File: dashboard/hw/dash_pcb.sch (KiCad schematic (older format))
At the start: 28 parts, among them J1 LCD, J2 DEBUG, J3 LCD_BL, J4 CAN, J5 POWER, U1 LPC11C24FBD48, U2 TPS62175

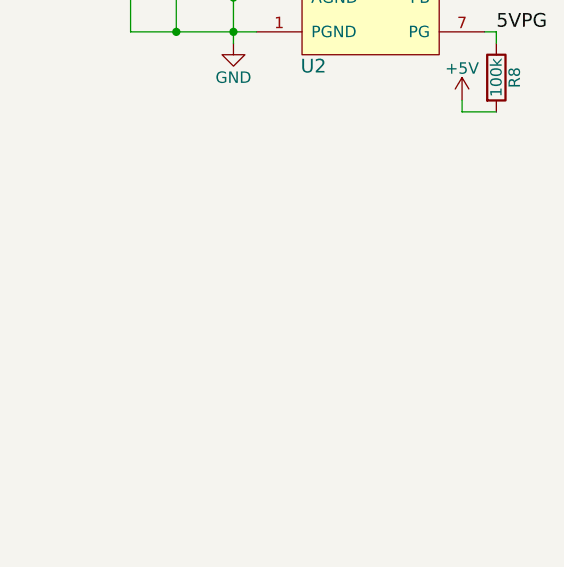
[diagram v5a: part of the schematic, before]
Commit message: add 3v3 power supply
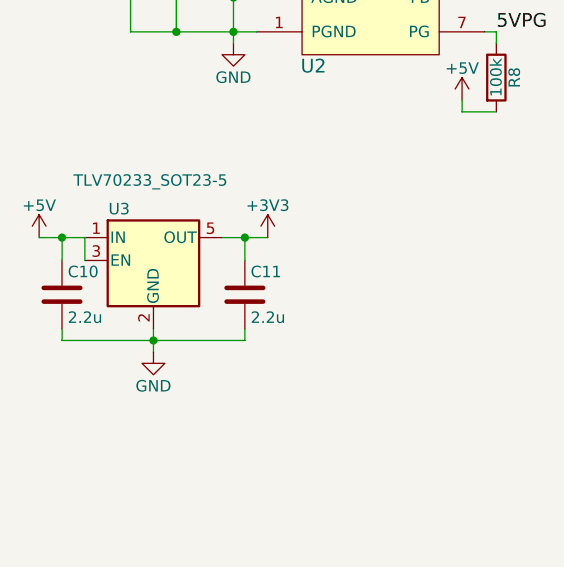
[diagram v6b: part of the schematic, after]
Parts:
- added C10, C11: 2.2u, Capacitors_SMD:C_0603, symbol C
- added U3: TLV70233_SOT23-5, TO_SOT_Packages_SMD:SOT-23-5, symbol TLV70233_SOT23-5
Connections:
- net +3V3: now also C11.1, U3.5 (OUT)
- net +5V: now also C10.1, U3.1 (IN), U3.3 (EN)
- net GND: now also C10.2, C11.2, U3.2 (GND)
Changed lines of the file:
@@
 $EndComp
 $Comp
-L GND #PWR16
+L GND #PWR19
 U 1 1 5ADCA1A0
 P 9250 2600
-F 0 "#PWR16" H 9250 2350 50  0001 C CNN
+F 0 "#PWR19" H 9250 2350 50  0001 C CNN
 F 1 "GND" H 9250 2450 50  0000 C CNN
 F 2 "" H 9250 2600 50  0001 C CNN
@@
 LCD_VEE
 $Comp
-L GND #PWR7
+L GND #PWR10
 U 1 1 5ADCA50B
 P 5450 5450
-F 0 "#PWR7" H 5450 5200 50  0001 C CNN
+F 0 "#PWR10" H 5450 5200 50  0001 C CNN
 F 1 "GND" H 5450 5300 50  0000 C CNN
 F 2 "" H 5450 5450 50  0001 C CNN
@@
 $EndComp
 $Comp
-L GND #PWR12
+L GND #PWR15
 U 1 1 5ADCA542
 P 7300 4850
-F 0 "#PWR12" H 7300 4600 50  0001 C CNN
+F 0 "#PWR15" H 7300 4600 50  0001 C CNN
 F 1 "GND" H 7300 4700 50  0000 C CNN
 F 2 "" H 7300 4850 50  0001 C CNN
@@
 $EndComp
 $Comp
-L +3V3 #PWR8
+L +3V3 #PWR11
 U 1 1 5ADCA654
 P 5600 1800
-F 0 "#PWR8" H 5600 1650 50  0001 C CNN
+F 0 "#PWR11" H 5600 1650 50  0001 C CNN
 F 1 "+3V3" H 5600 1940 50  0000 C CNN
 F 2 "" H 5600 1800 50  0001 C CNN
@@
 $EndComp
 $Comp
-L +5V #PWR11
+L +5V #PWR14
 U 1 1 5ADCA762
 P 7300 4550
-F 0 "#PWR11" H 7300 4400 50  0001 C CNN
+F 0 "#PWR14" H 7300 4400 50  0001 C CNN
 F 1 "+5V" H 7300 4690 50  0000 C CNN
 F 2 "" H 7300 4550 50  0001 C CNN
@@
 $EndComp
 $Comp
-L +3V3 #PWR18
+L +3V3 #PWR21
 U 1 1 5ADCAB0C
 P 9500 5650
-F 0 "#PWR18" H 9500 5500 50  0001 C CNN
+F 0 "#PWR21" H 9500 5500 50  0001 C CNN
 F 1 "+3V3" H 9500 5790 50  0000 C CNN
 F 2 "" H 9500 5650 50  0001 C CNN
@@
 $EndComp
 $Comp
-L GND #PWR17
+L GND #PWR20
 U 1 1 5ADCAB42
 P 9350 6300
-F 0 "#PWR17" H 9350 6050 50  0001 C CNN
+F 0 "#PWR20" H 9350 6050 50  0001 C CNN
 F 1 "GND" H 9350 6150 50  0000 C CNN
 F 2 "" H 9350 6300 50  0001 C CNN
@@
 CANL
 $Comp
-L +3V3 #PWR15
+L +3V3 #PWR18
 U 1 1 5AE5BC1B
 P 8800 2600
-F 0 "#PWR15" H 8800 2450 50  0001 C CNN
+F 0 "#PWR18" H 8800 2450 50  0001 C CNN
 F 1 "+3V3" H 8800 2740 50  0000 C CNN
 F 2 "" H 8800 2600 50  0001 C CNN
@@
 $EndComp
 $Comp
-L +3V3 #PWR14
+L +3V3 #PWR17
 U 1 1 5AE5BE05
 P 8450 3700
-F 0 "#PWR14" H 8450 3550 50  0001 C CNN
+F 0 "#PWR17" H 8450 3550 50  0001 C CNN
 F 1 "+3V3" H 8450 3840 50  0000 C CNN
 F 2 "" H 8450 3700 50  0001 C CNN
@@
 $EndComp
 $Comp
-L GND #PWR13
+L GND #PWR16
 U 1 1 5AE5BE6A
 P 8450 3100
-F 0 "#PWR13" H 8450 2850 50  0001 C CNN
+F 0 "#PWR16" H 8450 2850 50  0001 C CNN
 F 1 "GND" H 8450 2950 50  0000 C CNN
 F 2 "" H 8450 3100 50  0001 C CNN
@@
 $EndComp
 $Comp
-L GND #PWR21
+L GND #PWR24
 U 1 1 5AE5C42C
 P 10850 2800
-F 0 "#PWR21" H 10850 2550 50  0001 C CNN
+F 0 "#PWR24" H 10850 2550 50  0001 C CNN
 F 1 "GND" H 10850 2650 50  0000 C CNN
 F 2 "" H 10850 2800 50  0001 C CNN
@@
 $EndComp
 $Comp
-L GND #PWR19
+L GND #PWR22
 U 1 1 5AED81B0
 P 10000 4950
-F 0 "#PWR19" H 10000 4700 50  0001 C CNN
+F 0 "#PWR22" H 10000 4700 50  0001 C CNN
 F 1 "GND" H 10000 4800 50  0000 C CNN
 F 2 "" H 10000 4950 50  0001 C CNN
@@
 $EndComp
 $Comp
-L GND #PWR20
+L GND #PWR23
 U 1 1 5AED81E8
 P 10450 4450
-F 0 "#PWR20" H 10450 4200 50  0001 C CNN
+F 0 "#PWR23" H 10450 4200 50  0001 C CNN
 F 1 "GND" H 10450 4300 50  0000 C CNN
 F 2 "" H 10450 4450 50  0001 C CNN
@@
 $EndComp
 $Comp
-L GND #PWR10
+L GND #PWR13
 U 1 1 5AED9C6E
 P 6900 4400
-F 0 "#PWR10" H 6900 4150 50  0001 C CNN
+F 0 "#PWR13" H 6900 4150 50  0001 C CNN
 F 1 "GND" H 6900 4250 50  0000 C CNN
 F 2 "" H 6900 4400 50  0001 C CNN
@@
 $EndComp
 $Comp
-L GND #PWR9
+L GND #PWR12
 U 1 1 5AEDA2F6
 P 6050 2550
-F 0 "#PWR9" H 6050 2300 50  0001 C CNN
+F 0 "#PWR12" H 6050 2300 50  0001 C CNN
 F 1 "GND" H 6050 2400 50  0000 C CNN
 F 2 "" H 6050 2550 50  0001 C CNN
@@
 $EndComp
 $Comp
-L GND #PWR6
+L GND #PWR9
 U 1 1 5AEDA60D
 P 5050 2550
-F 0 "#PWR6" H 5050 2300 50  0001 C CNN
+F 0 "#PWR9" H 5050 2300 50  0001 C CNN
 F 1 "GND" H 5050 2400 50  0000 C CNN
 F 2 "" H 5050 2550 50  0001 C CNN
@@
 $EndComp
 $Comp
-L +3V3 #PWR4
+L +3V3 #PWR7
 U 1 1 5ADCA97A
 P 3550 2850
-F 0 "#PWR4" H 3550 2700 50  0001 C CNN
+F 0 "#PWR7" H 3550 2700 50  0001 C CNN
 F 1 "+3V3" H 3550 2990 50  0000 C CNN
 F 2 "" H 3550 2850 50  0001 C CNN
@@
 $EndComp
 $Comp
-L GND #PWR1
+L GND #PWR3
 U 1 1 5AF0114C
 P 1550 1550
-F 0 "#PWR1" H 1550 1300 50  0001 C CNN
+F 0 "#PWR3" H 1550 1300 50  0001 C CNN
 F 1 "GND" H 1550 1400 50  0000 C CNN
 F 2 "" H 1550 1550 50  0001 C CNN
@@
 $EndComp
 $Comp
-L +5V #PWR2
+L +5V #PWR5
 U 1 1 5AF017BC
 P 2550 1800
-F 0 "#PWR2" H 2550 1650 50  0001 C CNN
+F 0 "#PWR5" H 2550 1650 50  0001 C CNN
 F 1 "+5V" H 2550 1940 50  0000 C CNN
 F 2 "" H 2550 1800 50  0001 C CNN
@@
 $EndComp
 $Comp
-L +5V #PWR5
+L +5V #PWR8
 U 1 1 5AF01C77
 P 3650 750
-F 0 "#PWR5" H 3650 600 50  0001 C CNN
+F 0 "#PWR8" H 3650 600 50  0001 C CNN
 F 1 "+5V" H 3650 890 50  0000 C CNN
 F 2 "" H 3650 750 50  0001 C CNN
@@
 $EndComp
 $Comp
-L GND #PWR3
+L GND #PWR6
 U 1 1 5AF028D7
 P 3200 1550
-F 0 "#PWR3" H 3200 1300 50  0001 C CNN
+F 0 "#PWR6" H 3200 1300 50  0001 C CNN
 F 1 "GND" H 3200 1400 50  0000 C CNN
 F 2 "" H 3200 1550 50  0001 C CNN
@@
 Wire Wire Line
 	3450 1550 3200 1550
+$Comp
+L TLV70233_SOT23-5 U3
+U 1 1 5AF0174A
+P 1200 2500
+F 0 "U3" H 1050 2725 50  0000 C CNN
+F 1 "TLV70233_SOT23-5" H 850 2850 50  0000 L CNN
+F 2 "TO_SOT_Packages_SMD:SOT-23-5" H 1200 2825 50  0001 C CIN
+F 3 "https://www.mouser.de/ProductDetail/Texas-Instruments/TLV70233QDBVRQ1?qs=sGAEpiMZZMsGz1a6aV8DcHTv34nsPVHgey%2fBkWCnhrg%3d" H 1200 2550 50  0001 C CNN
+	1    1200 2500
+	1    0    0    -1
+$EndComp
+$Comp
+L GND #PWR2
+U 1 1 5AF0183D
+P 1200 2900
+F 0 "#PWR2" H 1200 2650 50  0001 C CNN
+F 1 "GND" H 1200 2750 50  0000 C CNN
+F 2 "" H 1200 2900 50  0001 C CNN
+F 3 "" H 1200 2900 50  0001 C CNN
+	1    1200 2900
+	1    0    0    -1
+$EndComp
+Wire Wire Line
+	1200 2800 1200 2900
+Wire Wire Line
+	900  2500 900  2400
+Wire Wire Line
+	900  2400 700  2400
+$Comp
+L +5V #PWR1
+U 1 1 5AF01B37
+P 700 2400
+F 0 "#PWR1" H 700 2250 50  0001 C CNN
+F 1 "+5V" H 700 2540 50  0000 C CNN
+F 2 "" H 700 2400 50  0001 C CNN
+F 3 "" H 700 2400 50  0001 C CNN
+	1    700  2400
+	1    0    0    -1
+$EndComp
+$Comp
+L C C10
+U 1 1 5AF01BBD
+P 800 2650
+F 0 "C10" H 825 2750 50  0000 L CNN
+F 1 "2.2u" H 825 2550 50  0000 L CNN
+F 2 "Capacitors_SMD:C_0603" H 838 2500 50  0001 C CNN
+F 3 "https://www.mouser.de/ProductDetail/Murata-Electronics/GRM188R61E225ME84D?qs=sGAEpiMZZMs0AnBnWHyRQKFZIQ7b73cdnYopqDynRzTqa0oaFCyatQ%3d%3d" H 800 2650 50  0001 C CNN
+	1    800  2650
+	1    0    0    -1
+$EndComp
+Wire Wire Line
+	800  2500 800  2400
+Connection ~ 800  2400
+Wire Wire Line
+	800  2800 800  2850
+Wire Wire Line
+	800  2850 1600 2850
+Connection ~ 1200 2850
+$Comp
+L C C11
+U 1 1 5AF01EAD
+P 1600 2650
+F 0 "C11" H 1625 2750 50  0000 L CNN
+F 1 "2.2u" H 1625 2550 50  0000 L CNN
+F 2 "Capacitors_SMD:C_0603" H 1638 2500 50  0001 C CNN
+F 3 "https://www.mouser.de/ProductDetail/Murata-Electronics/GRM188R61E225ME84D?qs=sGAEpiMZZMs0AnBnWHyRQKFZIQ7b73cdnYopqDynRzTqa0oaFCyatQ%3d%3d" H 1600 2650 50  0001 C CNN
+	1    1600 2650
+	1    0    0    -1
+$EndComp
+Wire Wire Line
+	1500 2400 1700 2400
+Wire Wire Line
+	1600 2400 1600 2500
+Wire Wire Line
+	1600 2850 1600 2800
+$Comp
+L +3V3 #PWR4
+U 1 1 5AF0216E
+P 1700 2400
+F 0 "#PWR4" H 1700 2250 50  0001 C CNN
+F 1 "+3V3" H 1700 2540 50  0000 C CNN
+F 2 "" H 1700 2400 50  0001 C CNN
+F 3 "" H 1700 2400 50  0001 C CNN
+	1    1700 2400
+	1    0    0    -1
+$EndComp
+Connection ~ 1600 2400
 $EndSCHEMATC

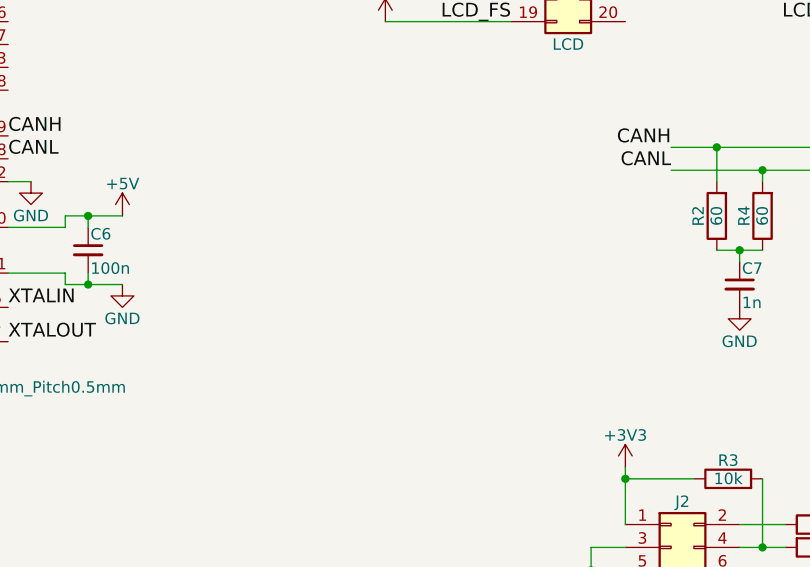
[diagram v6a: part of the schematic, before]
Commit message: add crystal to nxp
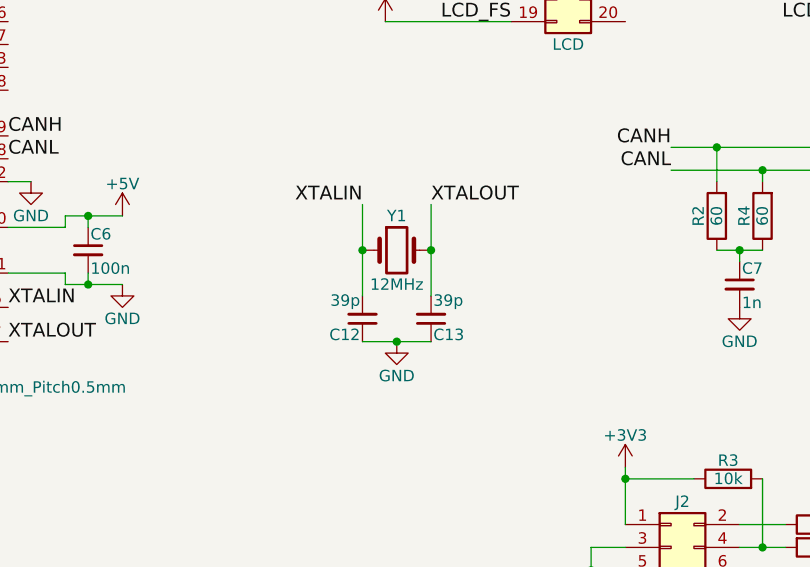
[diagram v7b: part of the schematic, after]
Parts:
- added C12, C13: 39p, Capacitors_SMD:C_0603, symbol C_Small
- added Y1: 12MHz, Crystals:Crystal_SMD_HC49-SD, symbol Crystal
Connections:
- net GND: now also C12.1, C13.1
- net XTALIN: now also C12.2, Y1.1
- net XTALOUT: now also C13.2, Y1.2
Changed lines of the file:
@@
 $EndComp
 $Comp
-L GND #PWR19
+L GND #PWR20
 U 1 1 5ADCA1A0
 P 9250 2600
-F 0 "#PWR19" H 9250 2350 50  0001 C CNN
+F 0 "#PWR20" H 9250 2350 50  0001 C CNN
 F 1 "GND" H 9250 2450 50  0000 C CNN
 F 2 "" H 9250 2600 50  0001 C CNN
@@
 $EndComp
 $Comp
-L +3V3 #PWR21
+L +3V3 #PWR22
 U 1 1 5ADCAB0C
 P 9500 5650
-F 0 "#PWR21" H 9500 5500 50  0001 C CNN
+F 0 "#PWR22" H 9500 5500 50  0001 C CNN
 F 1 "+3V3" H 9500 5790 50  0000 C CNN
 F 2 "" H 9500 5650 50  0001 C CNN
@@
 $EndComp
 $Comp
-L GND #PWR20
+L GND #PWR21
 U 1 1 5ADCAB42
 P 9350 6300
-F 0 "#PWR20" H 9350 6050 50  0001 C CNN
+F 0 "#PWR21" H 9350 6050 50  0001 C CNN
 F 1 "GND" H 9350 6150 50  0000 C CNN
 F 2 "" H 9350 6300 50  0001 C CNN
@@
 CANL
 $Comp
-L +3V3 #PWR18
+L +3V3 #PWR19
 U 1 1 5AE5BC1B
 P 8800 2600
-F 0 "#PWR18" H 8800 2450 50  0001 C CNN
+F 0 "#PWR19" H 8800 2450 50  0001 C CNN
 F 1 "+3V3" H 8800 2740 50  0000 C CNN
 F 2 "" H 8800 2600 50  0001 C CNN
@@
 $EndComp
 $Comp
-L GND #PWR24
+L GND #PWR25
 U 1 1 5AE5C42C
 P 10850 2800
-F 0 "#PWR24" H 10850 2550 50  0001 C CNN
+F 0 "#PWR25" H 10850 2550 50  0001 C CNN
 F 1 "GND" H 10850 2650 50  0000 C CNN
 F 2 "" H 10850 2800 50  0001 C CNN
@@
 $EndComp
 $Comp
-L GND #PWR22
+L GND #PWR23
 U 1 1 5AED81B0
 P 10000 4950
-F 0 "#PWR22" H 10000 4700 50  0001 C CNN
+F 0 "#PWR23" H 10000 4700 50  0001 C CNN
 F 1 "GND" H 10000 4800 50  0000 C CNN
 F 2 "" H 10000 4950 50  0001 C CNN
@@
 $EndComp
 $Comp
-L GND #PWR23
+L GND #PWR24
 U 1 1 5AED81E8
 P 10450 4450
-F 0 "#PWR23" H 10450 4200 50  0001 C CNN
+F 0 "#PWR24" H 10450 4200 50  0001 C CNN
 F 1 "GND" H 10450 4300 50  0000 C CNN
 F 2 "" H 10450 4450 50  0001 C CNN
@@
 $EndComp
 Connection ~ 1600 2400
+$Comp
+L Crystal Y1
+U 1 1 5AF03EF6
+P 8500 4700
+F 0 "Y1" H 8500 4850 50  0000 C CNN
+F 1 "12MHz" H 8500 4550 50  0000 C CNN
+F 2 "Crystals:Crystal_SMD_HC49-SD" H 8500 4700 50  0001 C CNN
+F 3 "https://www.mouser.de/ProductDetail/ABRACON/ABLS-12000MHZ-B2-T?qs=sGAEpiMZZMsBj6bBr9Q9aUe%252bp9Tek3UMlRk4loR5aNA%3d" H 8500 4700 50  0001 C CNN
+	1    8500 4700
+	1    0    0    -1
+$EndComp
+$Comp
+L C_Small C12
+U 1 1 5AF03D68
+P 8350 5000
+F 0 "C12" H 8360 5070 50  0000 L CNN
+F 1 "39p" H 8360 4920 50  0000 L CNN
+F 2 "Capacitors_SMD:C_0603" H 8350 5000 50  0001 C CNN
+F 3 "" H 8350 5000 50  0001 C CNN
+	1    8350 5000
+	-1   0    0    1
+$EndComp
+$Comp
+L C_Small C13
+U 1 1 5AF04127
+P 8650 5000
+F 0 "C13" H 8660 5070 50  0000 L CNN
+F 1 "39p" H 8660 4920 50  0000 L CNN
+F 2 "Capacitors_SMD:C_0603" H 8650 5000 50  0001 C CNN
+F 3 "" H 8650 5000 50  0001 C CNN
+	1    8650 5000
+	1    0    0    1
+$EndComp
+Wire Wire Line
+	8350 4500 8350 4900
+Wire Wire Line
+	8650 4500 8650 4900
+$Comp
+L GND #PWR18
+U 1 1 5AF045C8
+P 8500 5100
+F 0 "#PWR18" H 8500 4850 50  0001 C CNN
+F 1 "GND" H 8500 4950 50  0000 C CNN
+F 2 "" H 8500 5100 50  0001 C CNN
+F 3 "" H 8500 5100 50  0001 C CNN
+	1    8500 5100
+	1    0    0    -1
+$EndComp
+Wire Wire Line
+	8350 5100 8650 5100
+Connection ~ 8500 5100
+Connection ~ 8350 4700
+Connection ~ 8650 4700
+Text Label 8350 4500 2    60   ~ 0
+XTALIN
+Text Label 8650 4500 0    60   ~ 0
+XTALOUT
 $EndSCHEMATC

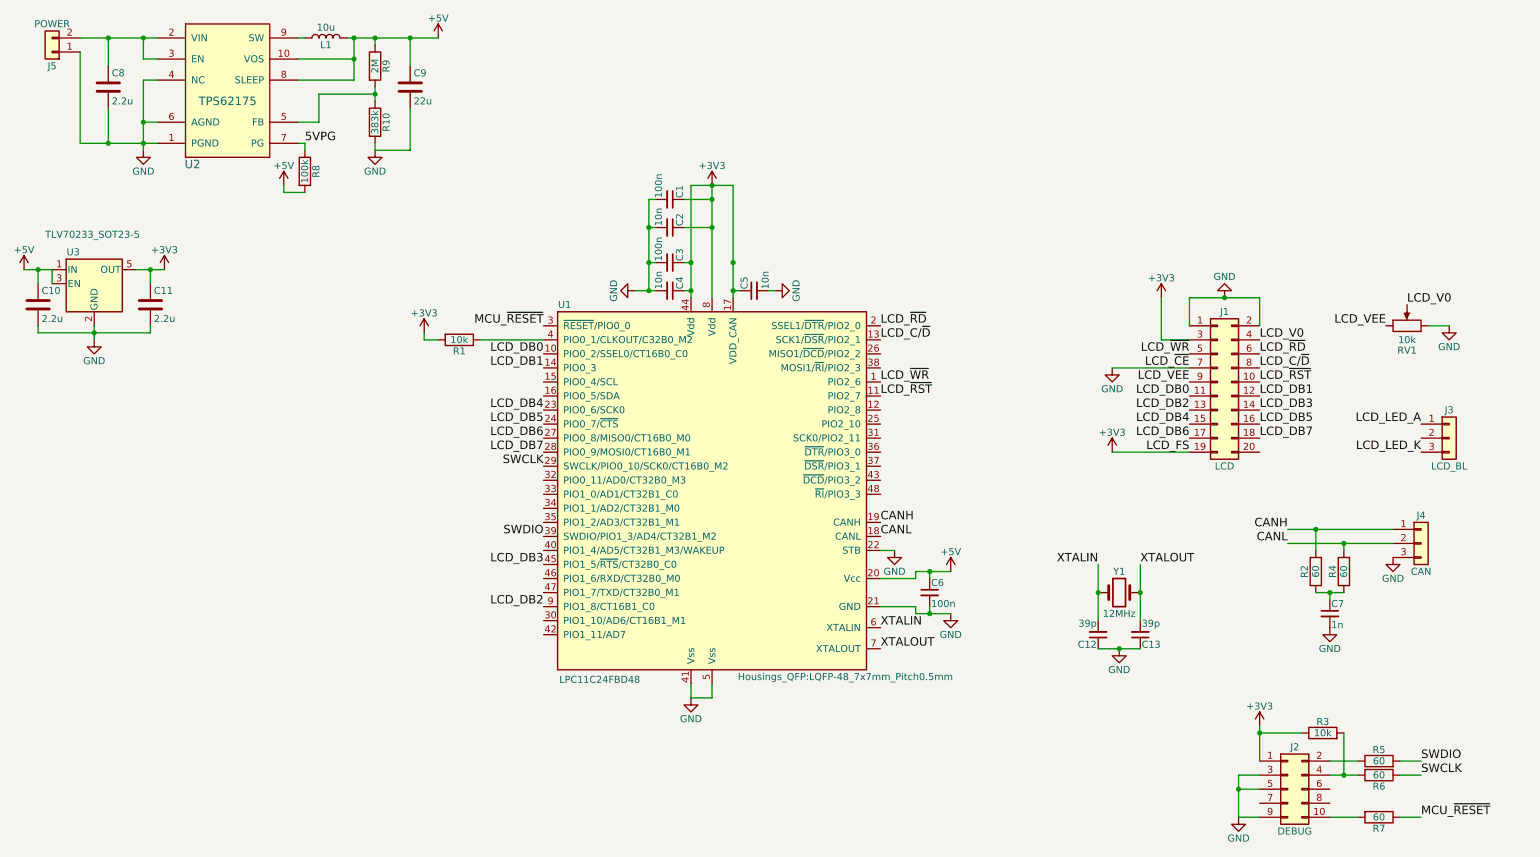
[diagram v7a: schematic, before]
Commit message: add led backlight 'driver'
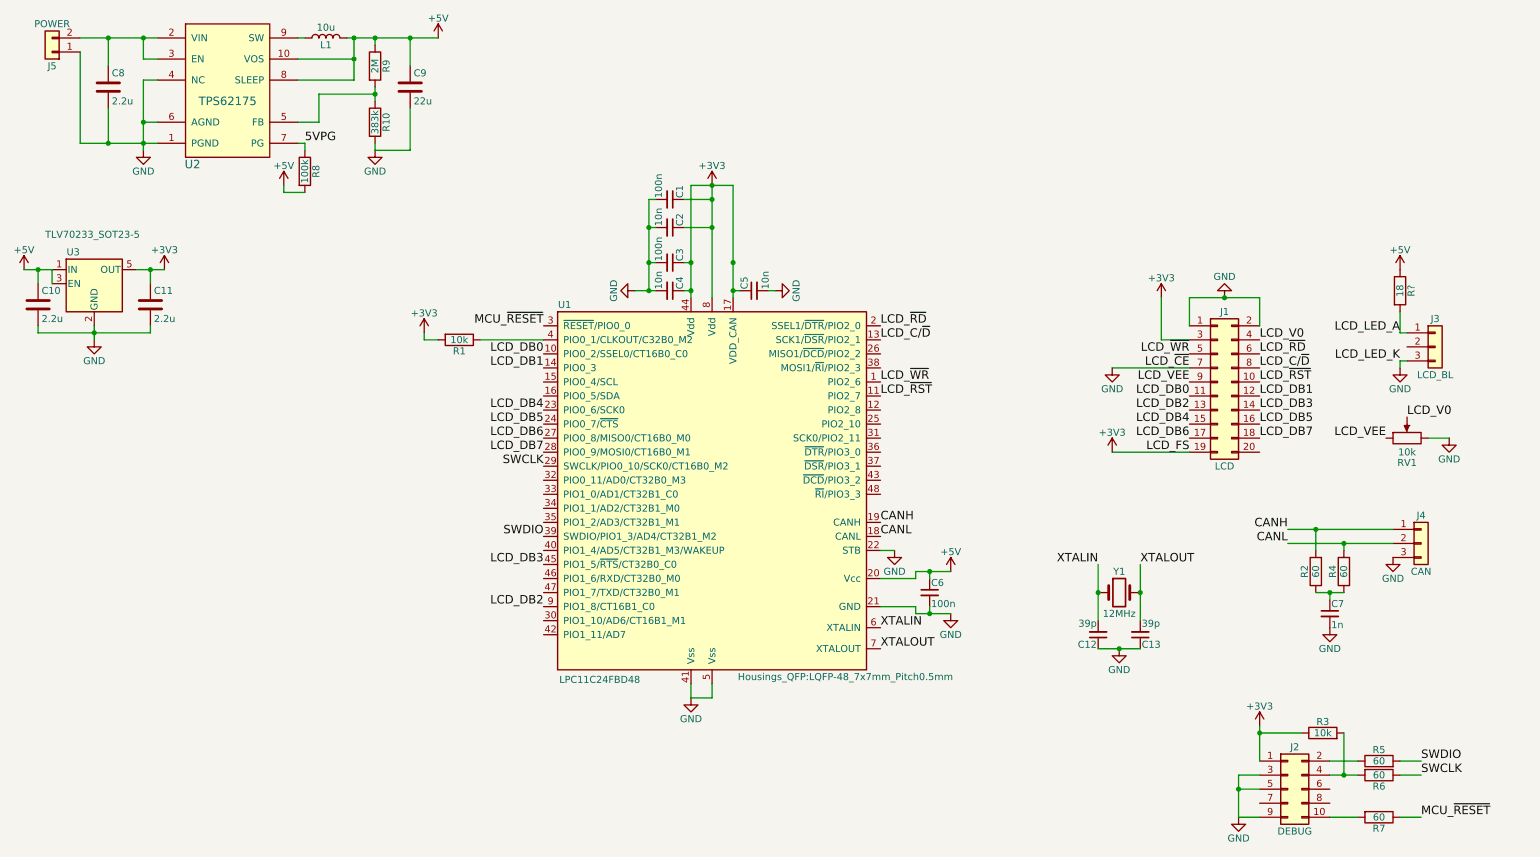
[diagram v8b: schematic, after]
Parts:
- added R?: 18, symbol R
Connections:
- net LCD_LED_K is gone; now on net GND: J3.3 (Pin_3)
- net +5V: now also R?.1
- net LCD_LED_A: now also R?.2
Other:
- moved on the sheet: J3, RV1
